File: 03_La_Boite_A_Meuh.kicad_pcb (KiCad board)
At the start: 2 copper layers, 100 x 100 mm, 4 parts

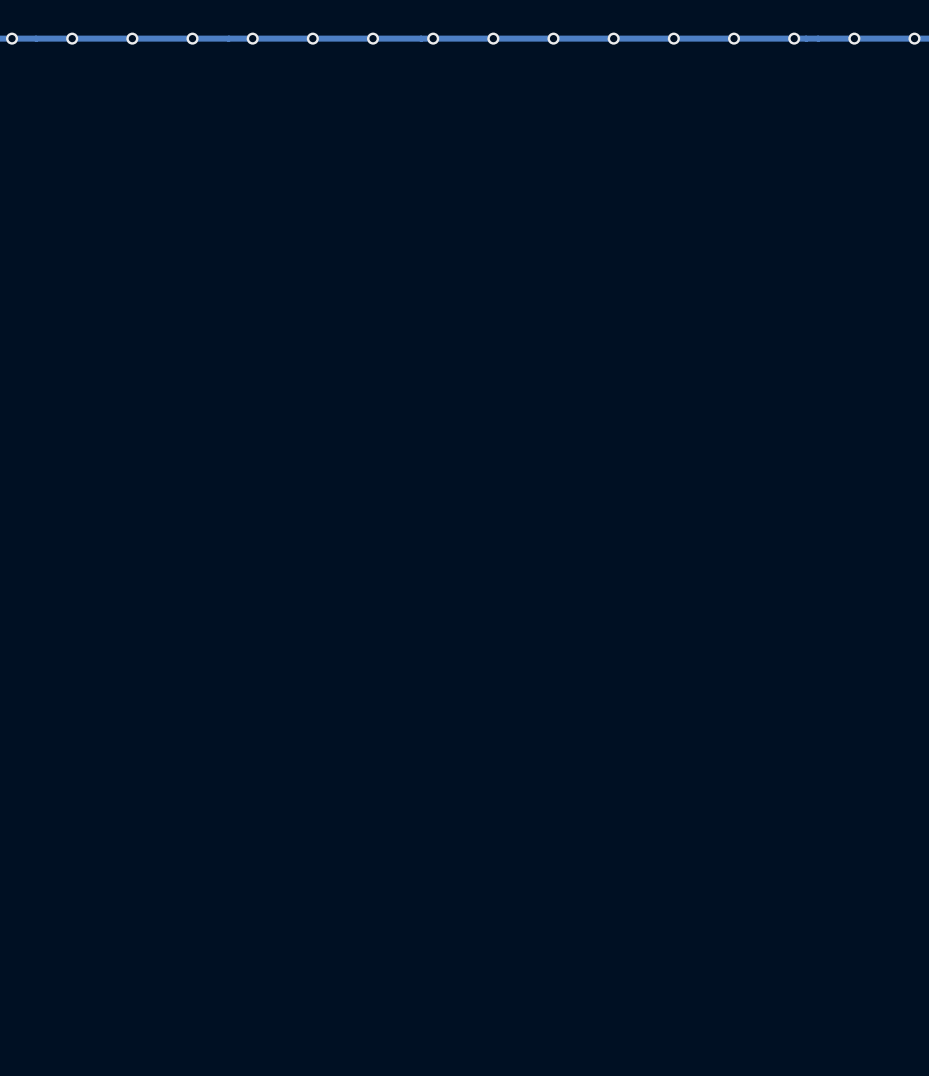
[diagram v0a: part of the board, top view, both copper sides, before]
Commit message: add esp32 && mp3 player
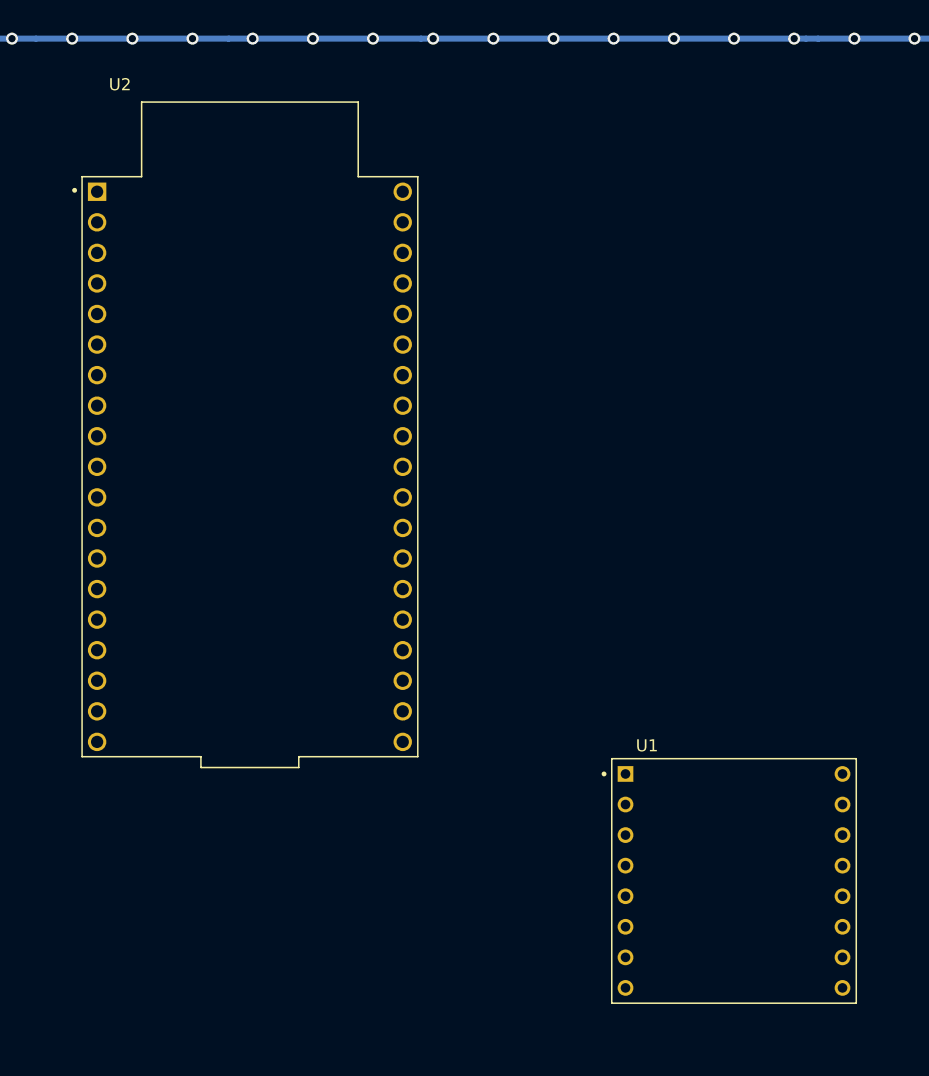
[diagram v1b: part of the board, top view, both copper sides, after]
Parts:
- added U1: DFR0299, Chimere:MODULE_DFR0299, F.Cu at (175.0, 130.0)
- added U2: ESP32-DEVKITC, Chimere:MODULE_ESP32-DEVKITC, F.Cu at (134.8, 95.6)

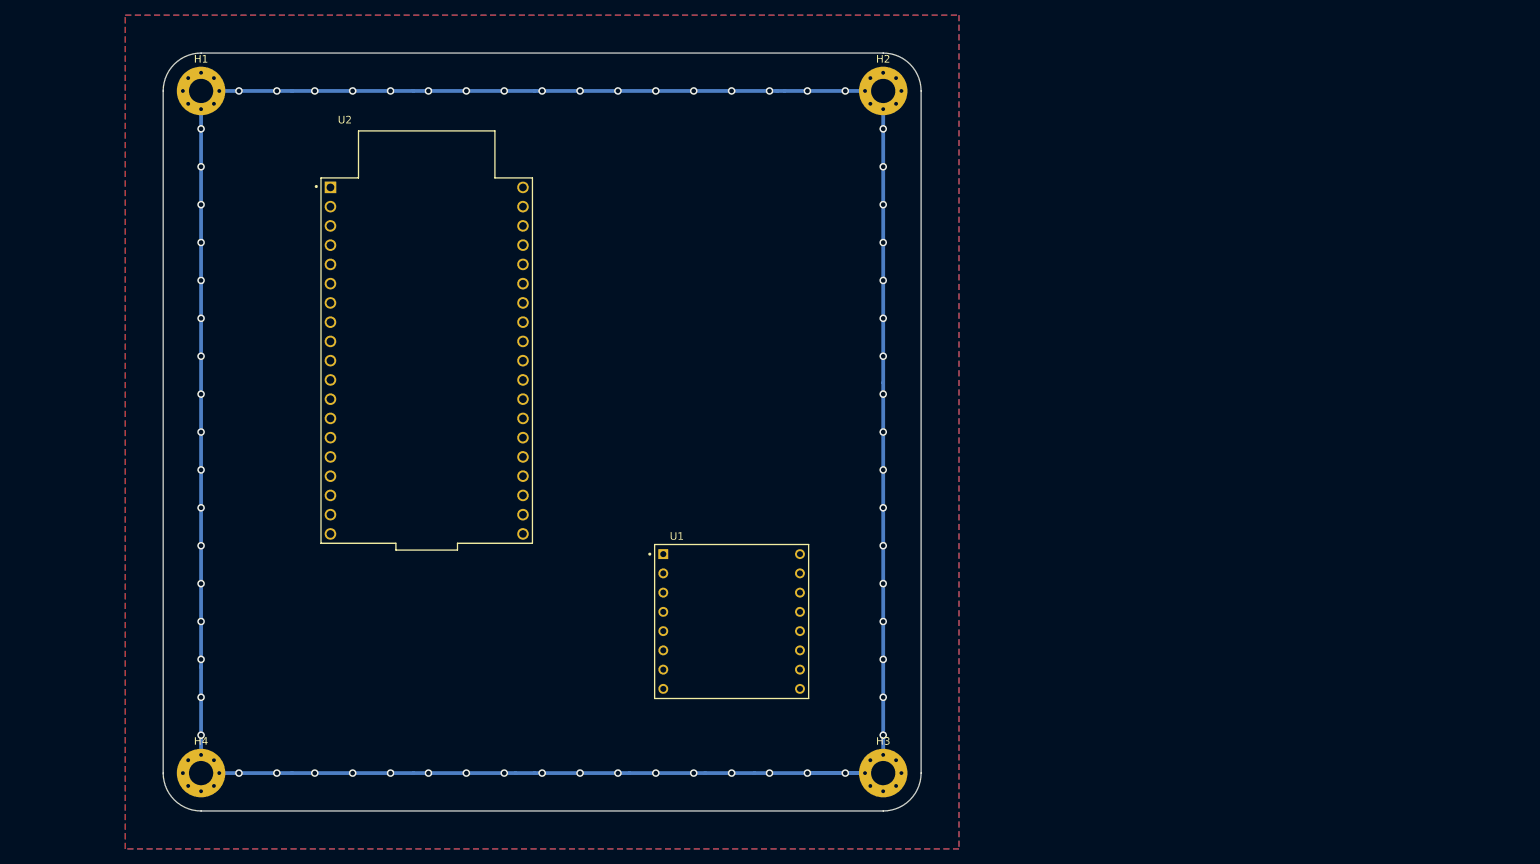
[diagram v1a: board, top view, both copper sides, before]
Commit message: fin schéma, début placement
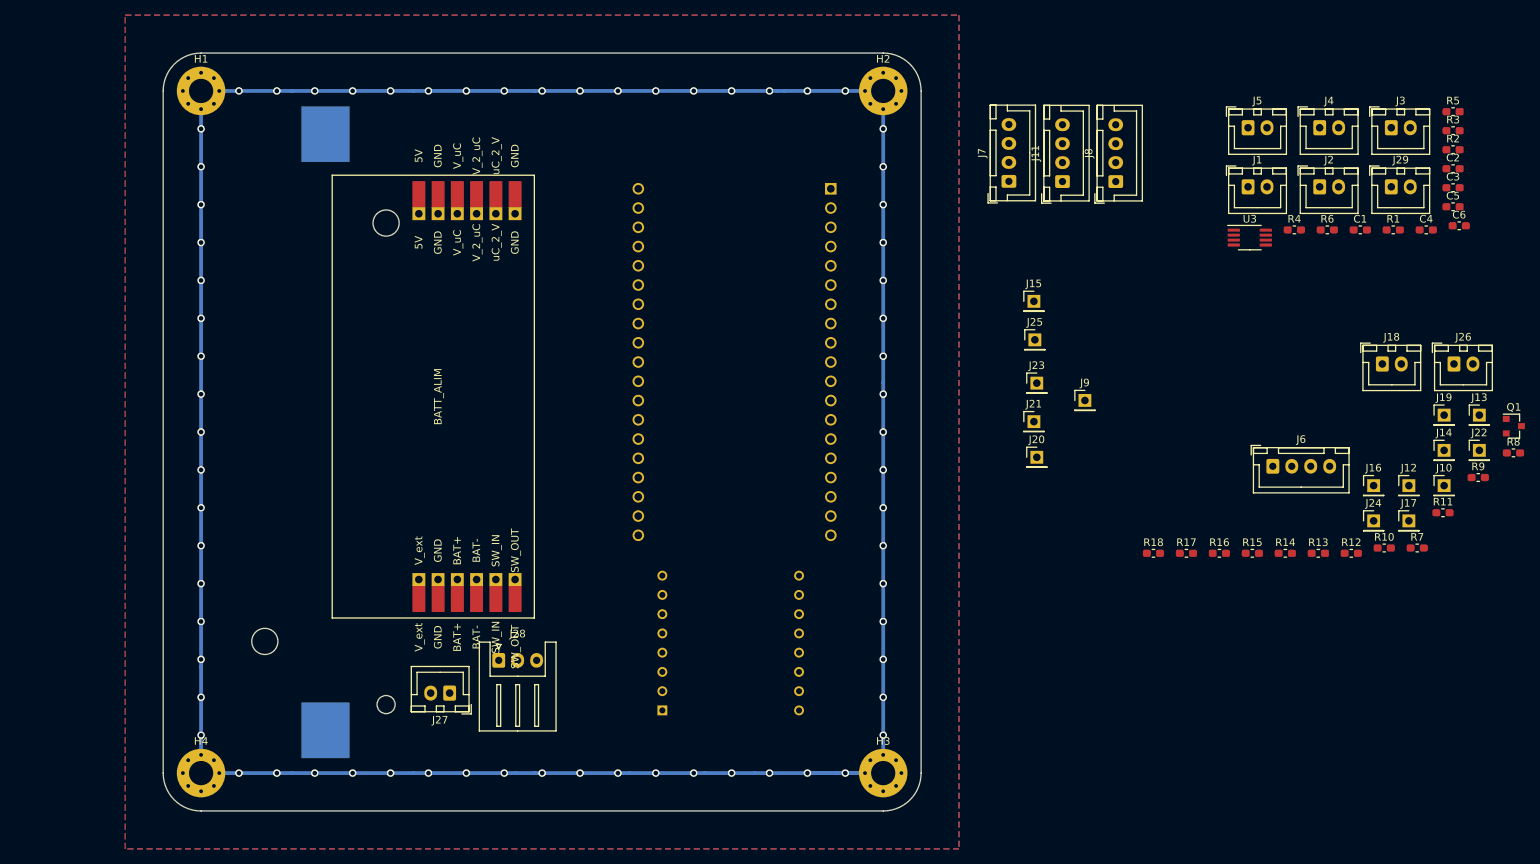
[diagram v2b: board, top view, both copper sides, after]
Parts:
- added BT1: Battery_Cell, Battery:BatteryHolder_Keystone_1042_1x18650, B.Cu at (121.4, 105.0)
- added C1: 1uF, Capacitor_SMD:C_0603_1608Metric_Pad1.05x0.95mm_HandSolder, F.Cu at (257.9, 78.3)
- added C2: 100nF, Capacitor_SMD:C_0603_1608Metric_Pad1.05x0.95mm_HandSolder, F.Cu at (270.2, 70.3)
- added C3: 100nF, Capacitor_SMD:C_0603_1608Metric_Pad1.05x0.95mm_HandSolder, F.Cu at (270.2, 72.8)
- added C4: 100nF, Capacitor_SMD:C_0603_1608Metric_Pad1.05x0.95mm_HandSolder, F.Cu at (266.6, 78.3)
- added C5: 100nF, Capacitor_SMD:C_0603_1608Metric_Pad1.05x0.95mm_HandSolder, F.Cu at (270.2, 75.3)
- added C6: 100nF, Capacitor_SMD:C_0603_1608Metric_Pad1.05x0.95mm_HandSolder, F.Cu at (271.0, 77.8)
- added J1: Conn_01x02, Connector_JST:JST_XH_B2B-XH-A_1x02_P2.50mm_Vertical, F.Cu at (243.1, 72.7)
- added J10: Conn_01x01, Connector_PinHeader_2.54mm:PinHeader_1x01_P2.54mm_Vertical, F.Cu at (269.0, 112.1)
- added J11: Conn_01x04, Connector_JST:JST_XH_B4B-XH-A_1x04_P2.50mm_Vertical, F.Cu at (218.7, 72.0)
- added J12: Conn_01x01, Connector_PinHeader_2.54mm:PinHeader_1x01_P2.54mm_Vertical, F.Cu at (264.4, 112.1)
- added J13: Conn_01x01, Connector_PinHeader_2.54mm:PinHeader_1x01_P2.54mm_Vertical, F.Cu at (273.7, 102.8)
- added J14: Conn_01x01, Connector_PinHeader_2.54mm:PinHeader_1x01_P2.54mm_Vertical, F.Cu at (269.0, 107.4)
- added J15: Conn_01x01, Connector_PinHeader_2.54mm:PinHeader_1x01_P2.54mm_Vertical, F.Cu at (214.9, 87.8)
- added J16: Conn_01x01, Connector_PinHeader_2.54mm:PinHeader_1x01_P2.54mm_Vertical, F.Cu at (259.7, 112.1)
- added J17: Conn_01x01, Connector_PinHeader_2.54mm:PinHeader_1x01_P2.54mm_Vertical, F.Cu at (264.4, 116.7)
- added J18: Conn_01x02, Connector_JST:JST_XH_B2B-XH-A_1x02_P2.50mm_Vertical, F.Cu at (260.9, 96.0)
- added J19: Conn_01x01, Connector_PinHeader_2.54mm:PinHeader_1x01_P2.54mm_Vertical, F.Cu at (269.0, 102.8)
- added J2: Conn_01x02, Connector_JST:JST_XH_B2B-XH-A_1x02_P2.50mm_Vertical, F.Cu at (252.6, 72.7)
- added J20: Conn_01x01, Connector_PinHeader_2.54mm:PinHeader_1x01_P2.54mm_Vertical, F.Cu at (215.3, 108.3)
- added J21: Conn_01x01, Connector_PinHeader_2.54mm:PinHeader_1x01_P2.54mm_Vertical, F.Cu at (214.9, 103.6)
- added J22: Conn_01x01, Connector_PinHeader_2.54mm:PinHeader_1x01_P2.54mm_Vertical, F.Cu at (273.7, 107.4)
- added J23: Conn_01x01, Connector_PinHeader_2.54mm:PinHeader_1x01_P2.54mm_Vertical, F.Cu at (215.3, 98.6)
- added J24: Conn_01x01, Connector_PinHeader_2.54mm:PinHeader_1x01_P2.54mm_Vertical, F.Cu at (259.7, 116.7)
- added J25: Conn_01x01, Connector_PinHeader_2.54mm:PinHeader_1x01_P2.54mm_Vertical, F.Cu at (215.0, 92.8)
- added J26: Conn_01x02, Connector_JST:JST_XH_B2B-XH-A_1x02_P2.50mm_Vertical, F.Cu at (270.3, 96.0)
- added J27: Conn_01x02, Connector_JST:JST_XH_B2B-XH-A_1x02_P2.50mm_Vertical, F.Cu at (137.8, 139.4)
- added J28: Conn_01x03, Connector_JST:JST_XH_S3B-XH-A_1x03_P2.50mm_Horizontal, F.Cu at (144.3, 135.1)
- added J29: Conn_01x02, Connector_JST:JST_XH_B2B-XH-A_1x02_P2.50mm_Vertical, F.Cu at (262.0, 72.7)
- added J3: Conn_01x02, Connector_JST:JST_XH_B2B-XH-A_1x02_P2.50mm_Vertical, F.Cu at (262.0, 64.9)
- added J4: Conn_01x02, Connector_JST:JST_XH_B2B-XH-A_1x02_P2.50mm_Vertical, F.Cu at (252.6, 64.9)
- added J5: Conn_01x02, Connector_JST:JST_XH_B2B-XH-A_1x02_P2.50mm_Vertical, F.Cu at (243.1, 64.9)
- added J6: Conn_01x04, Connector_JST:JST_XH_B4B-XH-A_1x04_P2.50mm_Vertical, F.Cu at (246.4, 109.5)
- added J7: Conn_01x04, Connector_JST:JST_XH_B4B-XH-A_1x04_P2.50mm_Vertical, F.Cu at (211.6, 71.9)
- added J8: Conn_01x04, Connector_JST:JST_XH_B4B-XH-A_1x04_P2.50mm_Vertical, F.Cu at (225.7, 72.0)
- added J9: Conn_01x01, Connector_PinHeader_2.54mm:PinHeader_1x01_P2.54mm_Vertical, F.Cu at (221.6, 100.8)
- added Q1: 2N7002, Package_TO_SOT_SMD:SOT-23, F.Cu at (278.2, 104.2)
- added R1: 100k, Resistor_SMD:R_0603_1608Metric_Pad1.05x0.95mm_HandSolder, F.Cu at (262.3, 78.3)
- added R10: 0, Resistor_SMD:R_0603_1608Metric_Pad1.05x0.95mm_HandSolder, F.Cu at (261.1, 120.3)
- added R11: 0, Resistor_SMD:R_0603_1608Metric_Pad1.05x0.95mm_HandSolder, F.Cu at (268.9, 115.7)
- added R12: 100k, Resistor_SMD:R_0603_1608Metric_Pad1.05x0.95mm_HandSolder, F.Cu at (256.8, 121.0)
- added R13: 10k, Resistor_SMD:R_0603_1608Metric_Pad1.05x0.95mm_HandSolder, F.Cu at (252.4, 121.0)
- added R14: 10k, Resistor_SMD:R_0603_1608Metric_Pad1.05x0.95mm_HandSolder, F.Cu at (248.1, 121.0)
- added R15: 22k, Resistor_SMD:R_0603_1608Metric_Pad1.05x0.95mm_HandSolder, F.Cu at (243.7, 121.0)
- added R16: 1k, Resistor_SMD:R_0603_1608Metric_Pad1.05x0.95mm_HandSolder, F.Cu at (239.4, 121.0)
- added R17: 100, Resistor_SMD:R_0603_1608Metric_Pad1.05x0.95mm_HandSolder, F.Cu at (235.0, 121.0)
- added R18: 100k, Resistor_SMD:R_0603_1608Metric_Pad1.05x0.95mm_HandSolder, F.Cu at (230.7, 121.0)
- added R2: 100k, Resistor_SMD:R_0603_1608Metric_Pad1.05x0.95mm_HandSolder, F.Cu at (270.2, 67.8)
- added R3: 0, Resistor_SMD:R_0603_1608Metric_Pad1.05x0.95mm_HandSolder, F.Cu at (270.2, 65.2)
- added R4: 100k, Resistor_SMD:R_0603_1608Metric_Pad1.05x0.95mm_HandSolder, F.Cu at (249.2, 78.3)
- added R5: 100k, Resistor_SMD:R_0603_1608Metric_Pad1.05x0.95mm_HandSolder, F.Cu at (270.2, 62.7)
- added R6: 100k, Resistor_SMD:R_0603_1608Metric_Pad1.05x0.95mm_HandSolder, F.Cu at (253.6, 78.3)
- added R7: 10k, Resistor_SMD:R_0603_1608Metric_Pad1.05x0.95mm_HandSolder, F.Cu at (265.5, 120.3)
- added R8: 2k2, Resistor_SMD:R_0603_1608Metric_Pad1.05x0.95mm_HandSolder, F.Cu at (278.2, 107.8)
- added R9: 2k2, Resistor_SMD:R_0603_1608Metric_Pad1.05x0.95mm_HandSolder, F.Cu at (273.5, 111.0)
- added U3: PAM8302AAS, Package_SO:MSOP-8_3x3mm_P0.65mm, F.Cu at (243.4, 79.4)
- added U4: Batt_Alim, Chimere:Batt_Alim, F.Cu at (133.7, 124.5)
- U1, U2: moved to B.Cu
- moved U2 40.6 mm to (175.4, 95.8), turned to 180 degrees
- moved U1 2.84 mm to (174.9, 132.8)
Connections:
- U1 pad 10: Net-(U1-Pad10) -> GND
- U1 pad 11: Net-(U1-Pad11) -> prev
- U1 pad 12: Net-(U1-Pad12) -> seg1
- U1 pad 13: Net-(U1-Pad13) -> seg5
- U1 pad 2: Net-(U1-Pad2) -> ESP2DFR
- U1 pad 3: Net-(U1-Pad3) -> DFR2ESP
- U1 pad 4: Net-(U1-Pad4) -> DFR_R
- U1 pad 5: Net-(U1-Pad5) -> DFR_L
- U1 pad 7: Net-(U1-Pad10) -> GND
- U1 pad 9: Net-(U1-Pad9) -> next
- U2 pad 1: Net-(U2-Pad1) -> 3V3
- U2 pad 14: Net-(U2-Pad14) -> GND
- U2 pad 19: Net-(U2-Pad19) -> 5V
- U2 pad 24: Net-(U2-Pad24) -> S0
- U2 pad 28: Net-(U2-Pad28) -> LED_out
- U2 pad 29: Net-(U2-Pad29) -> bouton1
- U2 pad 30: Net-(U2-Pad30) -> V_2_uC
- U2 pad 31: Net-(U2-Pad31) -> uC_2_V
- U2 pad 33: Net-(U2-Pad33) -> SDA
- U2 pad 36: Net-(U2-Pad36) -> SCL
- U2 pad 38: Net-(U2-Pad38) -> GND
- U2 pad 5: Net-(U2-Pad5) -> ESP_audio_out

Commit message: placement ok
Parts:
- moved Q1 131.0 mm to (148.0, 90.0), turned to 180 degrees
- moved J26 130.9 mm to (139.5, 91.0), turned to 180 degrees
- moved J3 130.3 mm to (156.0, 140.5)
- moved R8 121.9 mm to (159.5, 80.0)
- moved R9 120.2 mm to (159.5, 73.0)
- moved R11 115.8 mm to (159.5, 77.5)
- moved J18 112.8 mm to (149.0, 81.5)
- moved R10 111.2 mm to (159.5, 75.0)
- moved J5 110.9 mm to (156.0, 133.5)
- moved R12 110.6 mm to (151.5, 87.0), turned to 180 degrees
- moved J2 110.6 mm to (156.0, 126.5)
- moved C2 110.3 mm to (171.0, 118.5), turned to 90 degrees
- moved R3 106.9 mm to (179.9, 122.5)
- moved J29 106.2 mm to (166.0, 118.0), turned to 270 degrees
- moved R5 104.1 mm to (183.6, 120.5), turned to 180 degrees
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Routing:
- net Net-(BT1-Pad2): track 0.00 -> 68.2 mm
- net Net-(BT1-Pad1): track 0.00 -> 39.1 mm
- net GND: track 370.0 -> 385.0 mm, vias 68 -> 62
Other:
- outline, holes or cut-outs redrawn
- net class Default: clearance 0.3 -> 0.2
- rule trace_clearance: 0.3 -> 0.2

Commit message: routing + generation gerber
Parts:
- added REF**: KiCad-Logo2_5mm_SilkScreen, Symbol:KiCad-Logo2_5mm_SilkScreen, F.Cu at (120.0, 82.0)
- added REF**: OSHW-Logo2_7.3x6mm_SilkScreen, Symbol:OSHW-Logo2_7.3x6mm_SilkScreen, F.Cu at (120.0, 67.0)
- moved C6 25.0 mm to (187.5, 105.4)
- moved R6 25.0 mm to (187.5, 109.5)
- moved R10 7.02 mm to (166.5, 74.5)
- moved R11 5.50 mm to (165.0, 77.5)
- moved R14 4.36 mm to (151.0, 105.0)
- moved R3 3.92 mm to (183.5, 124.0), turned to 270 degrees
- moved R13 3.10 mm to (150.6, 99.0)
- moved R16 1.00 mm to (144.4, 90.0)
- moved R5 0.52 mm to (183.5, 120.0)
- moved C3 0.50 mm to (187.0, 118.0)
- moved J9 0.50 mm to (160.5, 69.5)
- moved C4 0.38 mm to (187.0, 132.0)
- moved C5 0.12 mm to (185.0, 132.0)
- moved R2 0.12 mm to (187.0, 128.0)
- turned R15 to 270 degrees
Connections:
- net Net-(J27-Pad2) renamed /Batt_alim/V_ext
- U4 pad 5: Net-(J28-Pad2) -> Net-(J28-Pad3)
- U4 pad 6: Net-(J28-Pad3) -> Net-(J28-Pad2)
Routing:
- net GND: track 385.0 -> 1137.1 mm, vias 62 -> 150
- net 3V3: track 0.00 -> 173.3 mm, vias 0 -> 5
- net 5V: track 0.00 -> 121.7 mm, vias 0 -> 2
- net ESP2DFR: track 0.00 -> 71.1 mm
- net DFR2ESP: track 0.00 -> 70.9 mm
- net uC_2_V: track 0.00 -> 36.8 mm, vias 0 -> 1
- net Net-(J28-Pad2): track 0.00 -> 35.3 mm
- net SCL: track 0.00 -> 33.9 mm
- net Net-(R2-Pad1): track 0.00 -> 33.6 mm
- net Net-(J28-Pad3): track 0.00 -> 32.2 mm
- net ESP_audio_out: track 0.00 -> 31.6 mm
- net SDA: track 0.00 -> 31.5 mm
- net V_2_uC: track 0.00 -> 30.0 mm, vias 0 -> 1
- net S0: track 0.00 -> 19.7 mm
- net seg5: track 0.00 -> 15.1 mm
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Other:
- net class fin added: clearance 0.2, trace_width 0.3, via_dia 1, via_drill 0.6
- net class gros added: clearance 0.2, trace_width 1, via_dia 1, via_drill 0.6
- board text added: "Bouton1"
- board text added: "I2C"
- board text added: "LED"
- board text added: "LEDS"
- board text added: "La boite à Meuh 2020 12 23"
- board text added: "SPK DFR"
- board text added: "SW"
- board text added: "Spk mix"
- board text added: "V_ext"
- board text added: "https://github.com/ThierryOrlandi/03_La_Boite_A_Meuh"
- board text added: "next"
- board text added: "prev"
- board text added: "seg1"
- board text added: "seg5"
